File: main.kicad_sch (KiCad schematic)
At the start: 0 parts

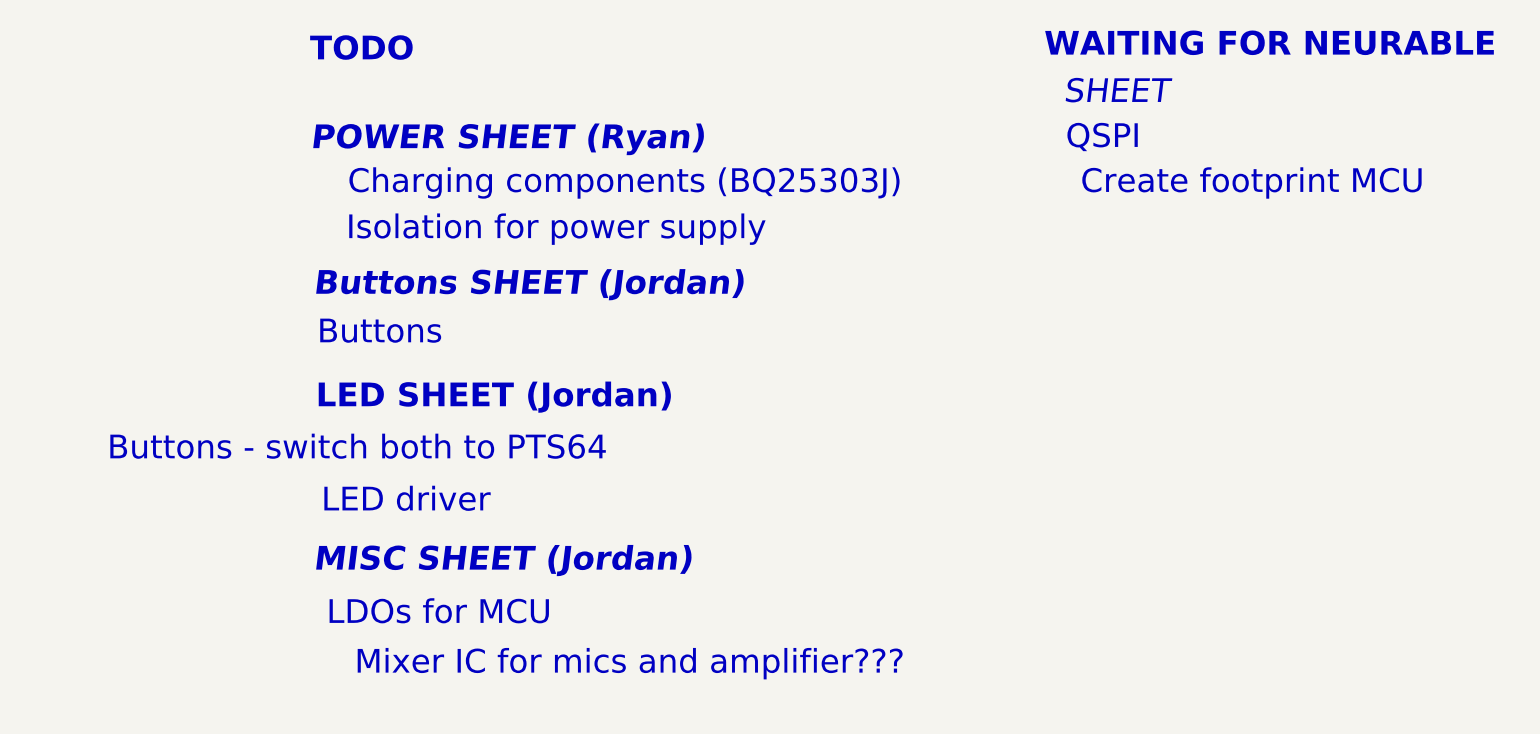
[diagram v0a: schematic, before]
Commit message: Add extra mounting hole. Relocate BM83 per Juan.
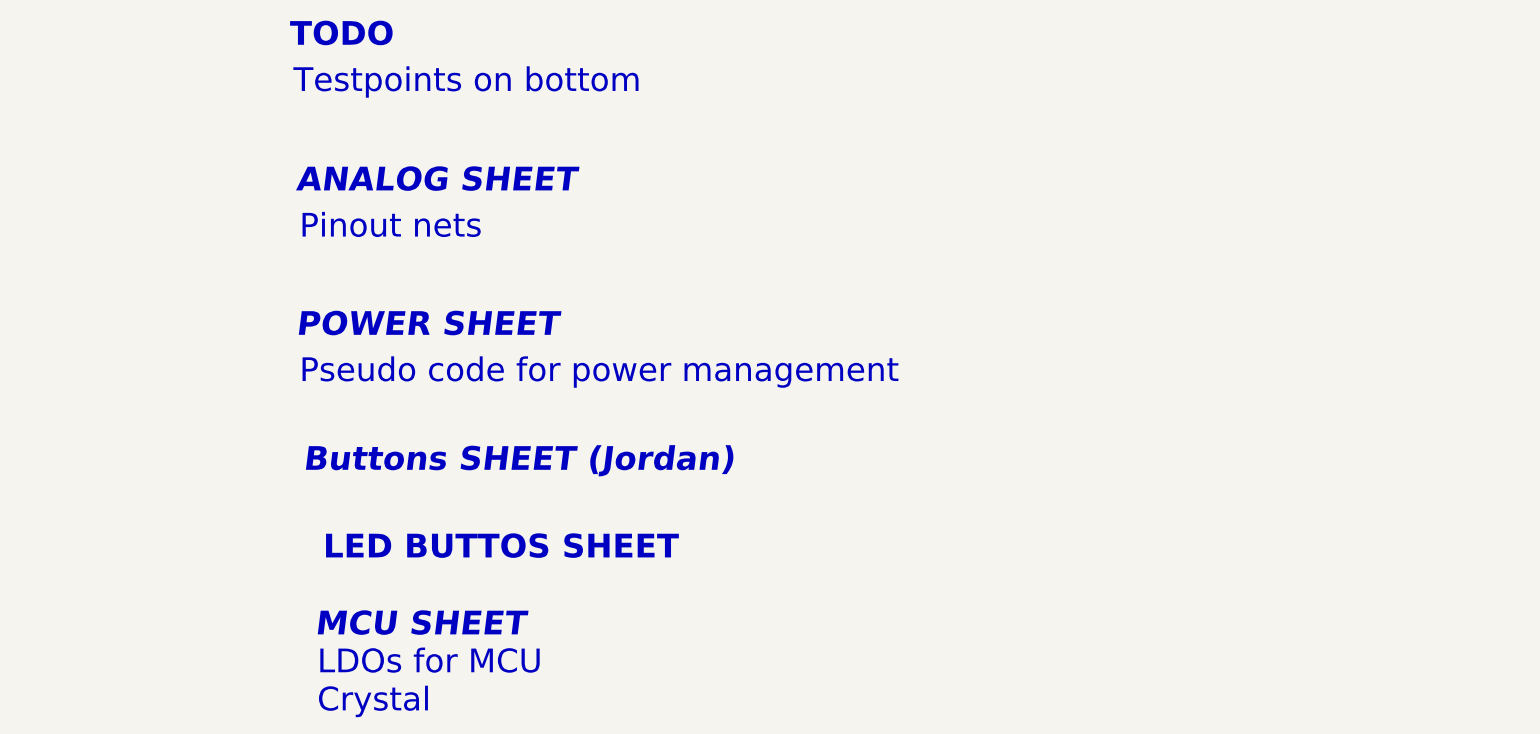
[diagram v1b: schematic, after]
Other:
- note added: "ANALOG SHEET"
- note added: "LDOs for MCU Crystal"
- note added: "LED BUTTOS SHEET"
- note added: "MCU SHEET"
- note added: "POWER SHEET"
- note added: "Pinout nets"
- note added: "Pseudo code for power management"
- note added: "Testpoints on bottom"
- note removed: "Buttons"
- note removed: "Buttons - switch both to PTS64"
- note removed: "Charging components (BQ25303J)"
- note removed: "Create footprint MCU"
- note removed: "Isolation for power supply"
- note removed: "LDOs for MCU"
- note removed: "LED SHEET (Jordan)"
- note removed: "LED driver"
- note removed: "MISC SHEET (Jordan)"
- note removed: "Mixer IC for mics and amplifier???"
- note removed: "POWER SHEET (Ryan)"
- note removed: "QSPI"
- note removed: "SHEET"
- note removed: "WAITING FOR NEURABLE"
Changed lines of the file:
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@@
 	(text "TODO"
 		(exclude_from_sim no)
-		(at 34.544 31.242 0)
+		(at 19.05 25.146 0)
 		(effects
 			(font
@@
 				(bold yes)
 			)
+			(justify left top)
 		)
 	)
-	(text "LED driver\n"
+	(text "LED BUTTOS SHEET"
 		(exclude_from_sim no)
-		(at 43.942 128.016 0)
-		(effects
-			(font
-				(size 5.08 5.08)
-			)
-		)
-	)
-	(text "WAITING FOR NEURABLE\n"
-		(exclude_from_sim no)
-		(at 229.362 30.226 0)
+		(at 26.162 135.128 0)
 		(effects
 			(font
@@
 				(bold yes)
 			)
+			(justify left top)
 		)
 	)
-	(text "SHEET"
+	(text "Pseudo code for power management"
 		(exclude_from_sim no)
-		(at 196.342 40.386 0)
-		(effects
-			(font
-				(size 5.08 5.08)
-				(italic yes)
-			)
-		)
-	)
-	(text "Buttons - switch both to PTS64\n"
-		(exclude_from_sim no)
-		(at 33.528 116.84 0)
+		(at 21.082 97.282 0)
 		(effects
 			(font
 				(size 5.08 5.08)
 			)
+			(justify left top)
 		)
 	)
-	(text "LED SHEET (Jordan)"
+	(text "MCU SHEET\n"
 		(exclude_from_sim no)
-		(at 62.992 105.664 0)
-		(effects
-			(font
-				(size 5.08 5.08)
-				(thickness 1.016)
-				(bold yes)
-			)
-		)
-	)
-	(text "Charging components (BQ25303J)\n"
-		(exclude_from_sim no)
-		(at 90.932 59.69 0)
-		(effects
-			(font
-				(size 5.08 5.08)
-			)
-		)
-	)
-	(text "QSPI\n"
-		(exclude_from_sim no)
-		(at 193.548 50.038 0)
-		(effects
-			(font
-				(size 5.08 5.08)
-			)
-		)
-	)
-	(text "MISC SHEET (Jordan)\n"
-		(exclude_from_sim no)
-		(at 64.77 140.716 0)
+		(at 24.384 151.638 0)
 		(effects
 			(font
@@
 				(italic yes)
 			)
+			(justify left top)
 		)
 	)
-	(text "Buttons\n"
+	(text "Pinout nets"
 		(exclude_from_sim no)
-		(at 38.354 91.948 0)
+		(at 21.082 66.294 0)
 		(effects
 			(font
 				(size 5.08 5.08)
 			)
+			(justify left top)
 		)
 	)
-	(text "Mixer IC for mics and amplifier???\n"
+	(text "Testpoints on bottom"
 		(exclude_from_sim no)
-		(at 91.948 162.814 0)
+		(at 19.812 35.052 0)
 		(effects
 			(font
 				(size 5.08 5.08)
 			)
+			(justify left top)
 		)
 	)
-	(text "LDOs for MCU\n"
+	(text "LDOs for MCU\nCrystal\n"
 		(exclude_from_sim no)
-		(at 51.054 152.146 0)
+		(at 24.892 159.766 0)
 		(effects
 			(font
 				(size 5.08 5.08)
 			)
+			(justify left top)
 		)
 	)
-	(text "Isolation for power supply\n"
+	(text "POWER SHEET"
 		(exclude_from_sim no)
-		(at 76.2 69.596 0)
-		(effects
-			(font
-				(size 5.08 5.08)
-			)
-		)
-	)
-	(text "POWER SHEET (Ryan)"
-		(exclude_from_sim no)
-		(at 65.786 50.292 0)
+		(at 20.32 87.376 0)
 		(effects
 			(font
@@
 				(italic yes)
 			)
+			(justify left top)
 		)
 	)
 	(text "Buttons SHEET (Jordan)"
 		(exclude_from_sim no)
-		(at 70.358 81.534 0)
+		(at 21.844 116.332 0)
 		(effects
 			(font
@@
 				(italic yes)
 			)
+			(justify left top)
 		)
 	)
-	(text "Create footprint MCU\n"
+	(text "ANALOG SHEET"
 		(exclude_from_sim no)
-		(at 225.552 59.69 0)
+		(at 20.32 56.388 0)
 		(effects
 			(font
 				(size 5.08 5.08)
+				(thickness 1.016)
+				(bold yes)
+				(italic yes)
 			)
+			(justify left top)
 		)
 	)
